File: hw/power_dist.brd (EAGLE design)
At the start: 80 x 50 mm, 82 parts, among them J1 JST-ZH6SMT_VERT, J2 JST-PH4SMT_VERT, J3 JST-PH5VERT, P1 XT30P, P2 XT30P, P3 XT30P, P4 XT30P, P5 XT30P, P6 XT30P, P7 XT90PW-M, Q1 PSMN4R8-100BSEJ, Q2 PSMN4R8-100BSEJ, Q3 PSMN4R8-100BSEJ, Q4 MF-DSC-SOT233-MMBT3904, Q5 MMBT5401 100V, U1 MAX15062AATA+T, U2 STM32G474CEU6, U4 TCAN334G, U5 LT1787HVIMS8PBF, U6 LTC4830

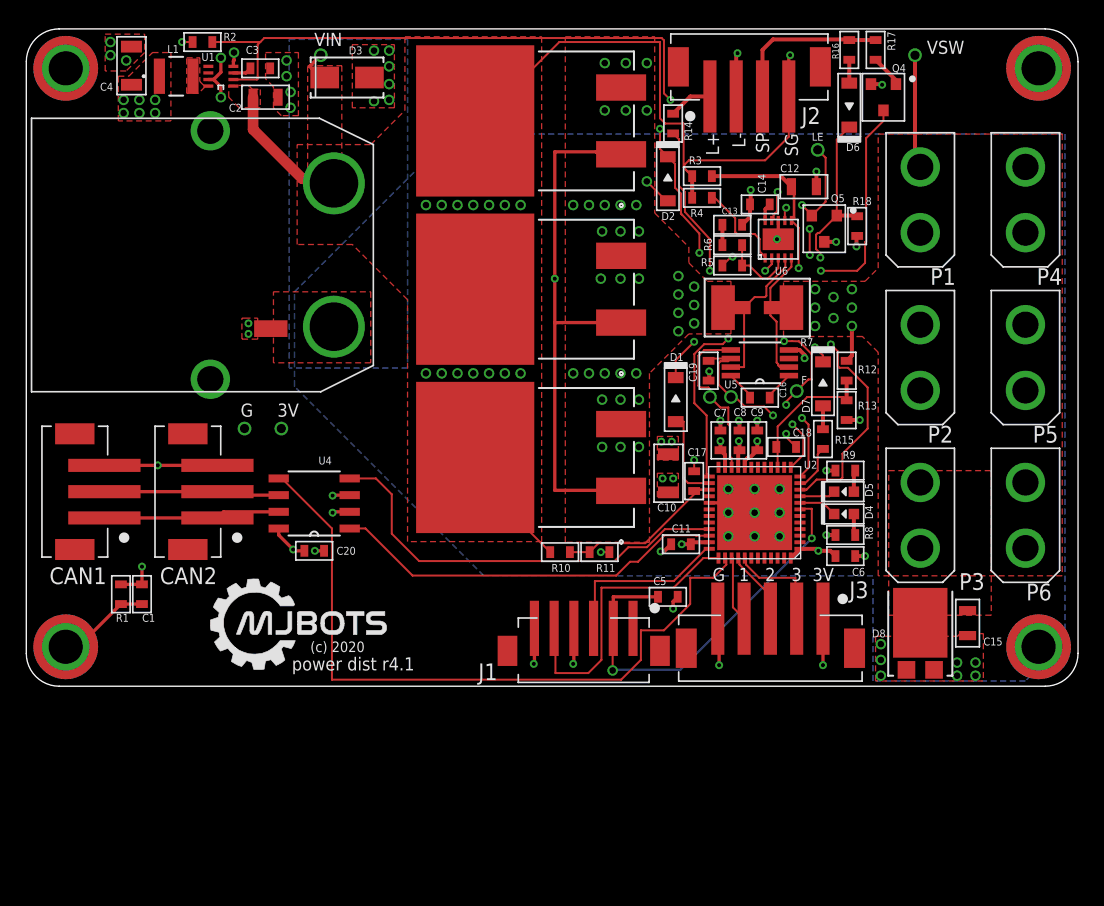
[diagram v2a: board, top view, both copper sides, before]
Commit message: Rough placement of r4.2 with the TPS2490
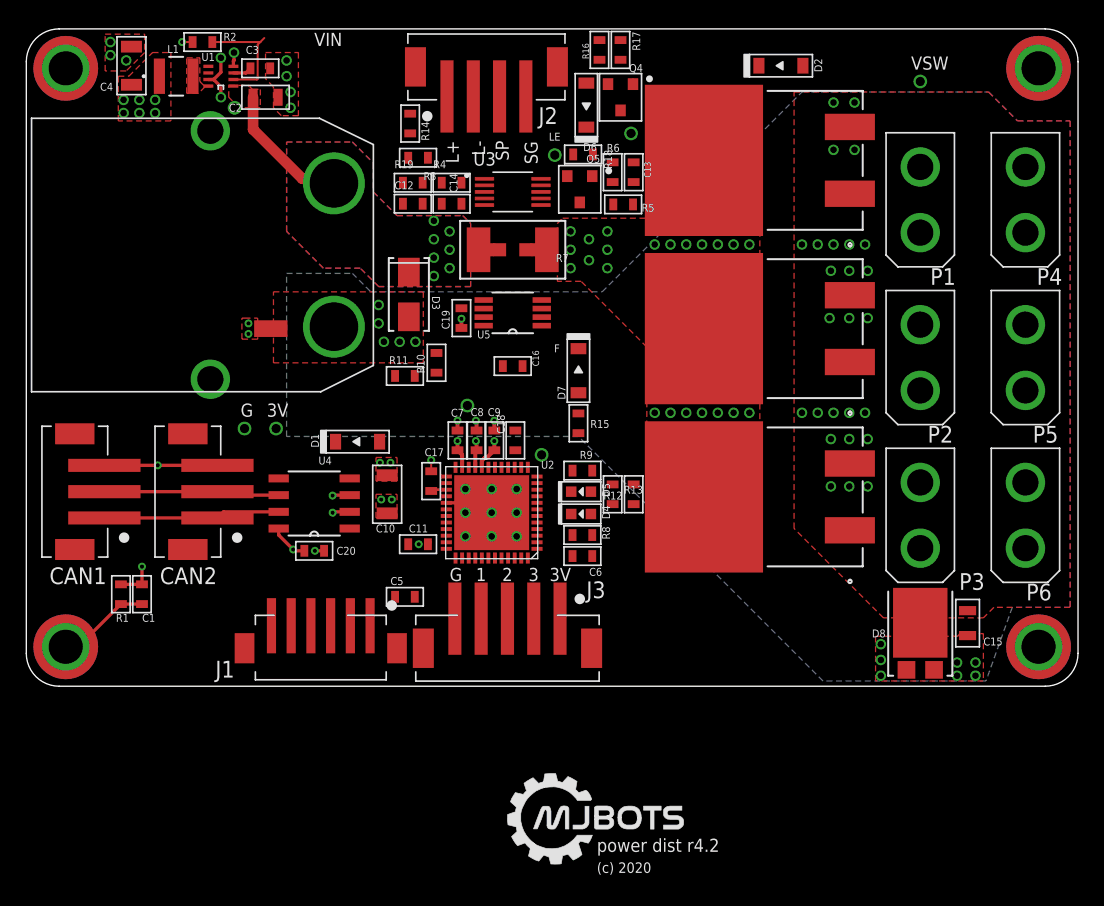
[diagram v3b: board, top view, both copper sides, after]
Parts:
- removed U6: LTC4830, power_dist:DFN10
- added R19: 6.8k 1%, mfpassives:R0603
- added U3: TPS2490DGSR, TPS2490DGSR:SOP50P490X110-10N
- C12: value 1uF 100V -> .1uF 100V; device mfpassives:C0805 -> mfpassives:C0603
- C13: value (none) -> 27nF
- C14: value 0.1uF -> 10nF
- R3: value 10k -> 2M
- R4: value (none) -> 47k 1%
- R5: value (none) -> 10
- R6: value (none) -> 1k
- moved C12 29.8 mm to (29.4, 36.7)
- moved D1 24.4 mm to (25.2, 18.6), turned to 0 degrees
- moved C14 23.5 mm to (32.4, 36.7)
- moved DB_FLT 23.3 mm to (46.0, 42.0)
- moved R3 21.6 mm to (29.8, 40.2), turned to 180 degrees
- moved R18 21.6 mm to (42.4, 40.5), turned to 0 degrees
- moved C10 21.5 mm to (27.4, 14.6)
- moved C18 20.6 mm to (37.2, 18.7), turned to 90 degrees
- moved DB_LEN 20.0 mm to (40.2, 40.4)
- moved J1 20.0 mm to (22.4, 2.60)
- moved R14 20.0 mm to (29.2, 42.8)
- moved C6 20.0 mm to (42.3, 9.90)
- moved C7 20.0 mm to (32.8, 18.7)
- moved C8 20.0 mm to (34.2, 18.7)
- moved C9 20.0 mm to (35.6, 18.7)
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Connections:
- removed net LTC_VCC: C12.P$1, R3.P$2, U6.2, U6.6
- removed net N$10: R4.P$1, U6.1
- removed net N$12: C14.P$1, U6.10
- removed net N$5: R5.P$1, R6.P$2, U6.3
- removed net VIN_POST: D2.ANODE, Q1.3, Q2.3, Q3.3, R7.1
- new net GDRV: R5.P$1, R6.P$2, U3.8
- new net PROG: R19.P$2, R4.P$1, U3.3
- new net TIMER: C14.P$1, U3.4
- new net VREF: R4.P$2, U3.2
- new net VSENSE: Q1.2, Q2.2, Q3.2, R7.2
- net +24V: now also C12.P$1, R3.P$2, R7.1; no longer Q1.2, Q2.2, Q3.2, R3.P$1, R4.P$2
- net FLT: now also U3.6; no longer U6.7
- net GND: now also R19.P$1, U3.5; no longer U6.8, U6.P$1
- net LTC_EN: now also R3.P$1, U3.1; no longer U6.9
- net VSENSE_HIGH: now also U3.10; no longer U6.4
- net VSENSE_LOW: now also U3.9; no longer U6.5
- net VSWITCHED: now also D2.ANODE, Q1.3, Q2.3, Q3.3, U3.7; no longer R7.2
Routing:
- net 3V3_EN: track 71.0 -> 8.83 mm, vias 4 -> 0
- net +24V: track 69.0 -> 10.3 mm, vias 15 -> 7
- net GATE: track 56.3 -> 0.06 mm, vias 2 -> 0
- net CAN_SHDN: track 54.1 -> 0.10 mm
- net SNS_PWR_SW: track 40.3 -> 0.00 mm, vias 2 -> 0
- net CAN_RX: track 32.7 -> 0.00 mm
- net PWR_LED: track 31.5 -> 0.00 mm, vias 2 -> 0
- net NRST: track 31.5 -> 0.23 mm, vias 2 -> 0
- net CAN_TX: track 30.1 -> 0.01 mm
- net FLT: track 26.3 -> 0.00 mm, vias 6 -> 0
- net GND: track 51.3 -> 26.2 mm, vias 48 -> 32
- net N$13: track 22.7 -> 0.00 mm, vias 2 -> 0
- net SWCLK: track 22.7 -> 0.18 mm
- net LTC_VCC: track 16.9 -> 0.00 mm, vias 2 -> 0
- net ISAMP_BIAS: track 16.9 -> 0.25 mm, vias 2 -> 0
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- added copper zone on layer 15, net +24V
- added copper zone on layer 16, net +24V
- added copper zone on layer 1, net VSENSE
- added copper zone on layer 2, net VSENSE
- removed copper zone on layer 1, net VIN_POST
- removed copper zone on layer 2, net VIN_POST
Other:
- board text added: "power dist r4.2"
- board text removed: "power dist r4.1"

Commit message: r4.2 everything rough routed
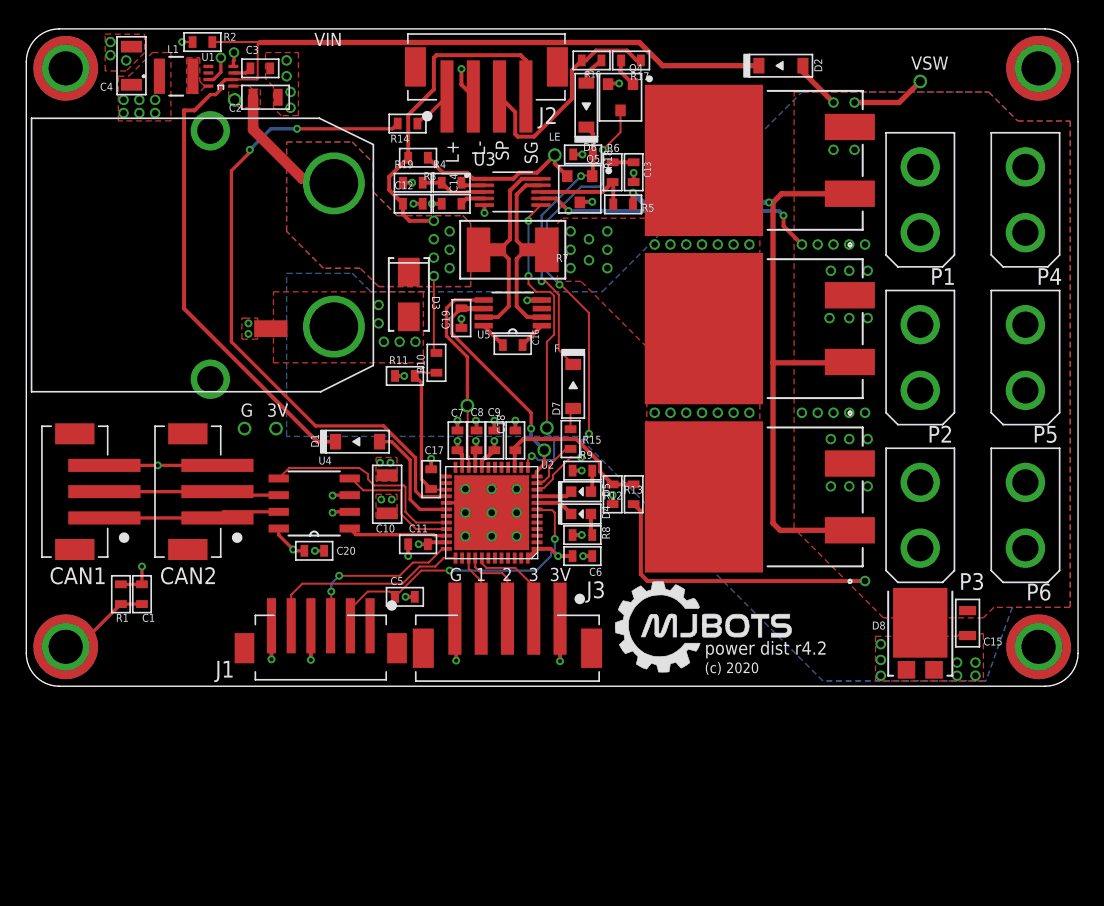
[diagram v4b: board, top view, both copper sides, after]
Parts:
- moved DB_FLT 23.3 mm to (39.6, 19.6)
- moved C16 1.60 mm to (37.0, 25.9)
- moved R15 1.34 mm to (41.4, 18.8)
- moved D7 1.26 mm to (41.6, 22.8)
- moved R17 1.13 mm to (46.0, 47.6), turned to 0 degrees
- moved R16 1.00 mm to (43.0, 47.6), turned to 180 degrees
- moved DB_VIN 0.60 mm to (15.8, 44.6)
- moved DB_IB 0.40 mm to (39.4, 17.9)
- moved R14 0.20 mm to (29.0, 42.8), turned to 180 degrees
- moved C17 0.15 mm to (30.8, 15.8)
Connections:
- net 3V3_OVERRIDE: now also U2.30; no longer U2.26
- net CAN_SHDN: now also U2.32; no longer U2.38
- net PWR_LED: now also U2.28; no longer U2.25
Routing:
- net 3V3_EN: track 8.83 -> 82.8 mm
- net GATE: track 0.06 -> 54.3 mm, vias 0 -> 2
- net VSWITCHED: track 0.00 -> 54.0 mm, vias 26 -> 29
- net PWR_LED: track 0.00 -> 50.0 mm, vias 0 -> 2
- net SNS_PWR_SW: track 0.00 -> 35.7 mm, vias 0 -> 4
- net +24V: track 10.3 -> 42.5 mm
- net FLT: track 0.00 -> 24.5 mm, vias 0 -> 3
- net NRST: track 0.23 -> 23.5 mm, vias 0 -> 2
- net N$13: track 0.00 -> 21.6 mm, vias 0 -> 2
- net GND: track 26.2 -> 44.3 mm, vias 32 -> 49
- net ISAMP_BIAS: track 0.25 -> 18.0 mm, vias 0 -> 1
- net PWR_SW: track 0.07 -> 17.3 mm
- net CAN_SHDN: track 0.10 -> 16.1 mm
- net ISAMP: track 0.00 -> 15.9 mm
- net SWCLK: track 0.18 -> 16.0 mm
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
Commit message: Connect TIMER to an ADC and add a FET temperature sensor
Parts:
- added C21: 0.1uF, mfpassives:C0603
- added U6: STLM20DD9FUDFN-4L_STM-L, power_dist:UDFN-4L_STM-L
- moved DB_FLT 0.40 mm to (39.6, 20.1)
- moved R12 0.15 mm to (46.0, 14.6)
- moved R13 0.05 mm to (44.5, 14.6)
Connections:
- new net FET_TEMP: U2.16, U6.1
- net GND: now also C21.P$2, U6.3
- net TIMER: now also U2.24
- net VCC: now also C21.P$1, U6.4
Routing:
- net FET_TEMP: track 0.00 -> 32.2 mm
- net TIMER: track 1.92 -> 28.2 mm, vias 0 -> 2
- net GND: track 44.3 -> 64.6 mm, vias 49 -> 51
- net VCC: track 23.0 -> 40.7 mm, vias 20 -> 22
- net VSWITCHED: track 54.0 -> 56.2 mm

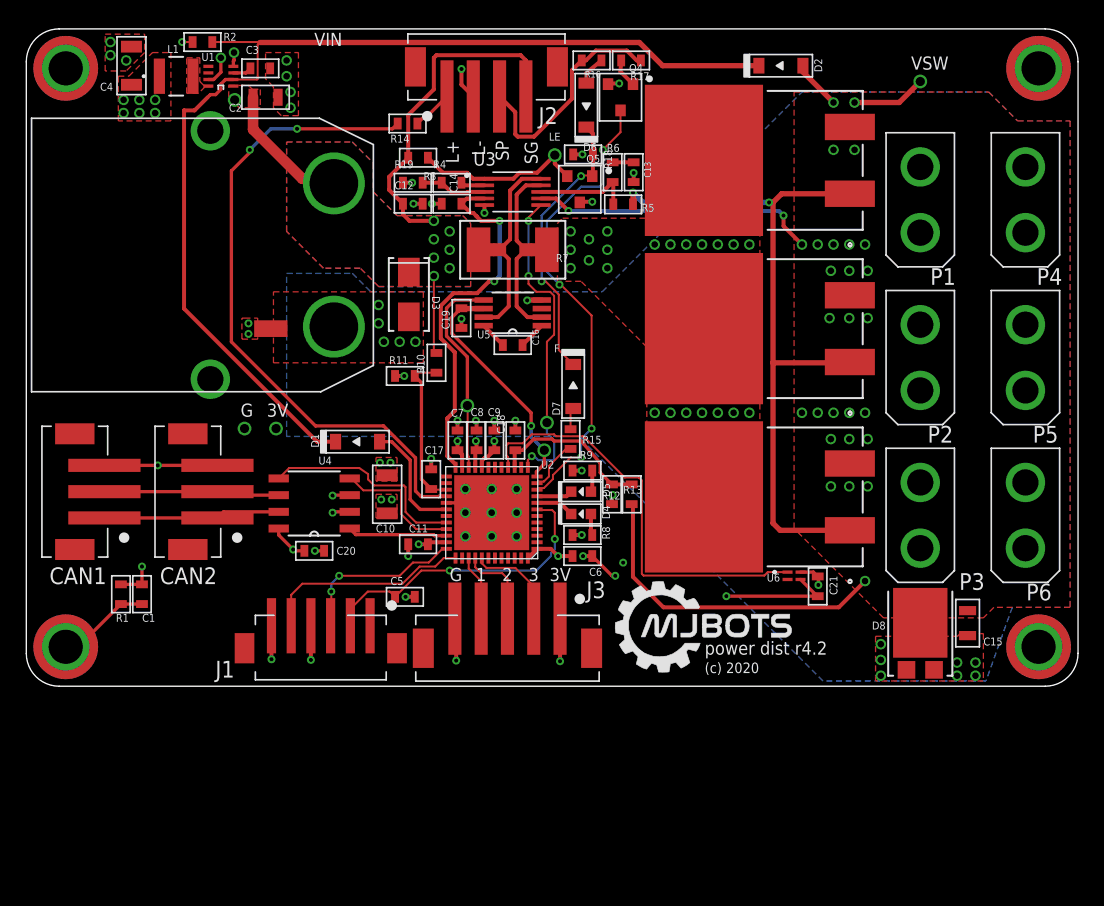
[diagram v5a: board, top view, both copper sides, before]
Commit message: Renumber all resistors and caps
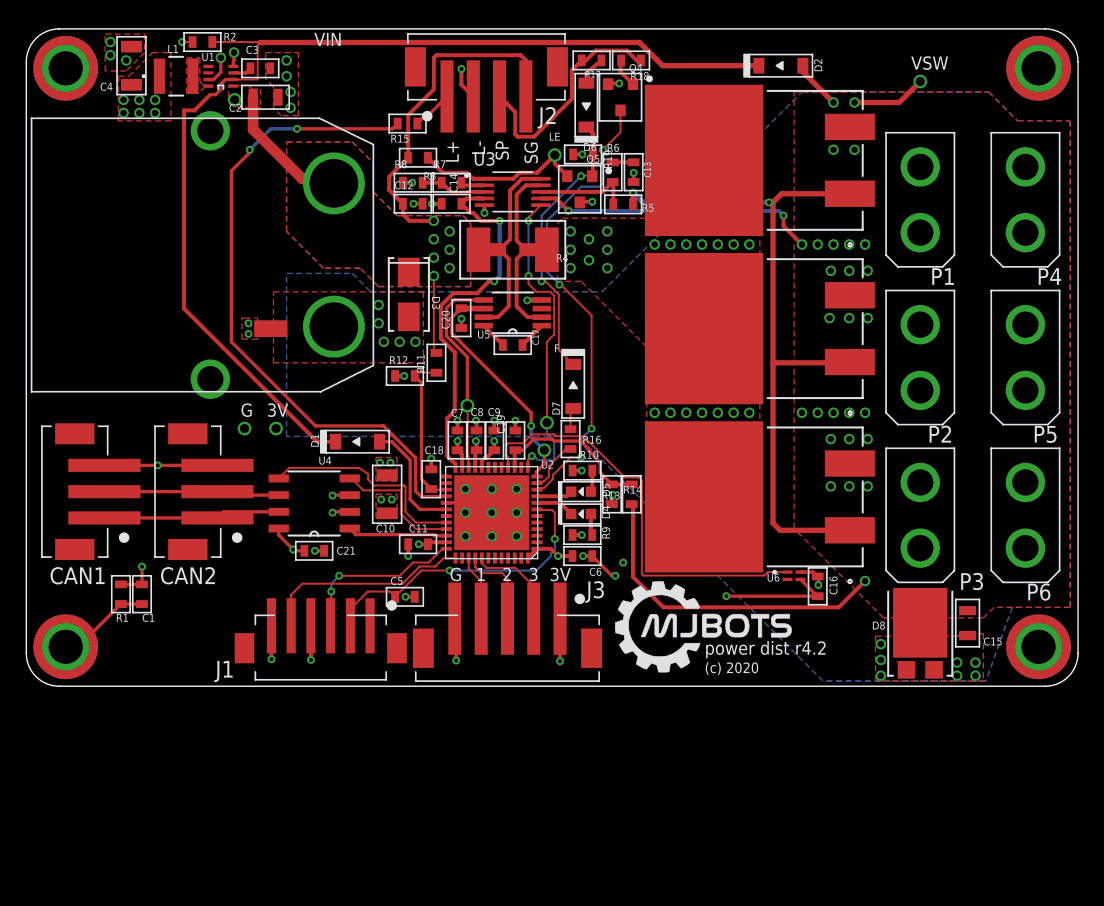
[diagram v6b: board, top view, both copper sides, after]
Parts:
- C16: value DNP -> 0.1uF
- C17: value 0.01uF -> DNP
- C19: value 0.1uF -> 0.01uF
- R10: value 3M 1% -> 220
- R11, R13: value 200k 1% -> 3M 1%
- R12: value 3M 1% -> 200k 1%
- R14: value 220 -> 200k 1%
- R15: value 1k -> 220
- R16: value 500k -> 1k
- R17: value 2M -> 500k
- R18: value 200k -> 2M
- R19: value 6.8k 1% -> 200k
- R4: value 47k 1% -> 0.5mOhm; device mfpassives:R0603 -> power_dist:SHUNT2512
- R7: value 0.5mOhm -> 47k 1%; device power_dist:SHUNT2512 -> mfpassives:R0603
- R8: value 220 -> 6.8k 1%
- moved C21 38.4 mm to (21.9, 10.3), turned to 180 degrees
- moved R14 32.2 mm to (44.5, 14.6), turned to 90 degrees
- moved R8 29.7 mm to (29.4, 38.3), turned to 0 degrees
- moved C16 29.6 mm to (60.2, 7.60), turned to 270 degrees
- moved R16 28.8 mm to (41.4, 18.8), turned to 270 degrees
- moved R15 27.0 mm to (29.0, 42.8), turned to 180 degrees
- moved C20 20.9 mm to (33.1, 28.0), turned to 270 degrees
- moved R12 19.5 mm to (28.8, 23.6), turned to 0 degrees
- moved R10 13.8 mm to (42.3, 16.4), turned to 180 degrees
- moved R19 13.1 mm to (42.4, 40.5)
- moved C17 11.9 mm to (37.0, 25.9), turned to 180 degrees
- moved C19 10.2 mm to (37.2, 18.7), turned to 90 degrees
- moved R18 8.03 mm to (46.0, 47.6)
- moved C18 7.05 mm to (30.8, 15.8)
- moved R4 6.90 mm to (37.0, 33.2)
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- renumbered SH4 to SH1
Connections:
- net +24V: now also R11.P$2, R4.1; no longer R10.P$2, R7.1
- net GND: now also C16.P$2, R12.P$1, R14.P$1, R8.P$1; no longer C17.P$2, R11.P$1, R13.P$1, R18.P$1
- net ISAMP_BIAS: now also C20.P$1; no longer C19.P$1
- net N$11: now also R18.P$1; no longer R17.P$1
- net N$13: now also R19.P$2; no longer R18.P$2
- net N$14: now also R10.P$1; no longer R9.P$1
- net N$17: now also R17.P$1; no longer R16.P$1
- net N$18: now also R16.P$1; no longer R15.P$1
- net N$2: now also R15.P$1; no longer R14.P$1
- net N$6: now also C17.P$1; no longer C16.P$1
- net N$7: now also C17.P$2; no longer C16.P$2
- net N$8: now also R9.P$1; no longer R8.P$1
- net PROG: now also R7.P$1, R8.P$2; no longer R19.P$2, R4.P$1
- net PWR_LED: now also R15.P$2; no longer R14.P$2
- net PWR_OVERRIDE: now also R16.P$2; no longer R15.P$2
- net PWR_SW: now also R18.P$2; no longer R16.P$2
- net VCC: now also C16.P$1, R10.P$2; no longer C20.P$1, R8.P$2
- net VIN_SAMP: now also C18.P$1, R11.P$1, R12.P$2; no longer C17.P$1, R10.P$1, R11.P$2
- net VREF: now also R7.P$2; no longer R4.P$2
- net VSENSE: now also R4.2; no longer R7.2
- net VSENSE_HIGH: now also R4.3; no longer R7.3
- net VSENSE_LOW: now also R4.4; no longer R7.4
- net VSWITCHED: now also R13.P$2; no longer R12.P$2
- net VSWITCHED_SAMP: now also C19.P$1, R13.P$1, R14.P$2; no longer C18.P$1, R12.P$1, R13.P$2

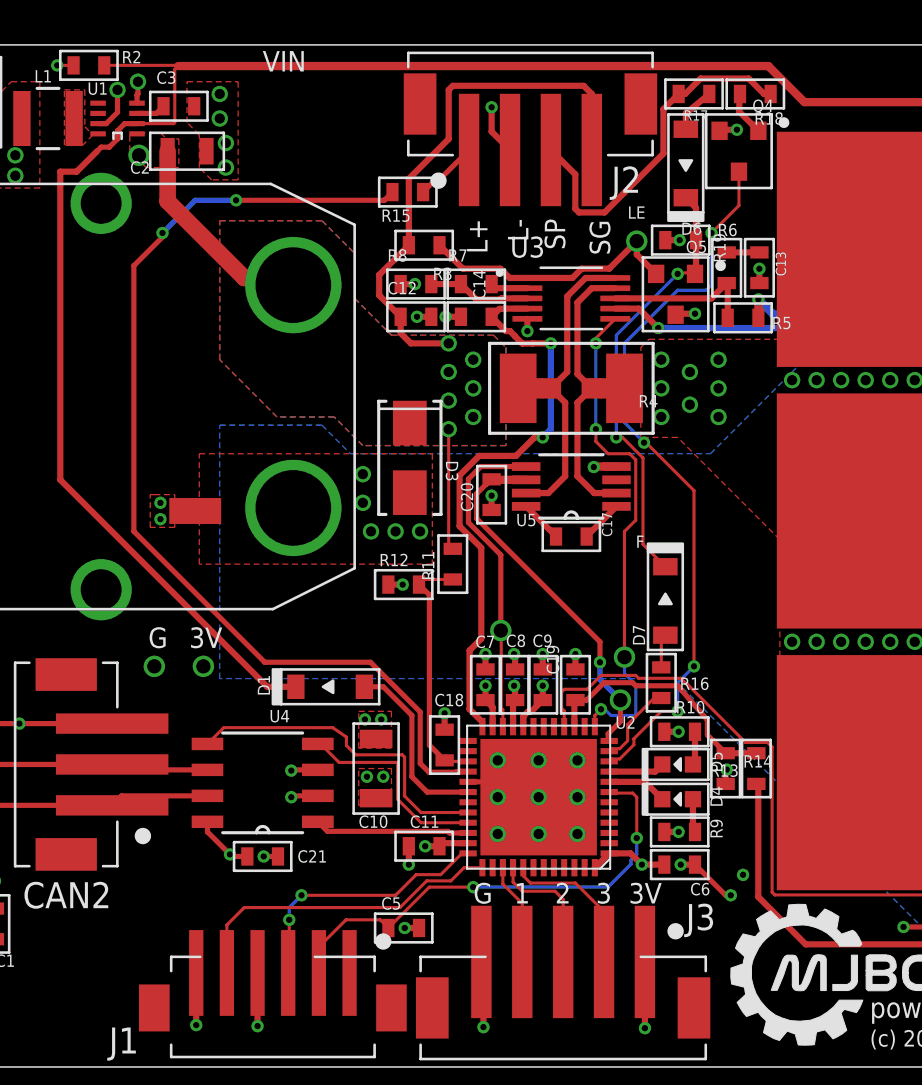
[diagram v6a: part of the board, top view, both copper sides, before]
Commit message: Place all silks and add a few more debug points
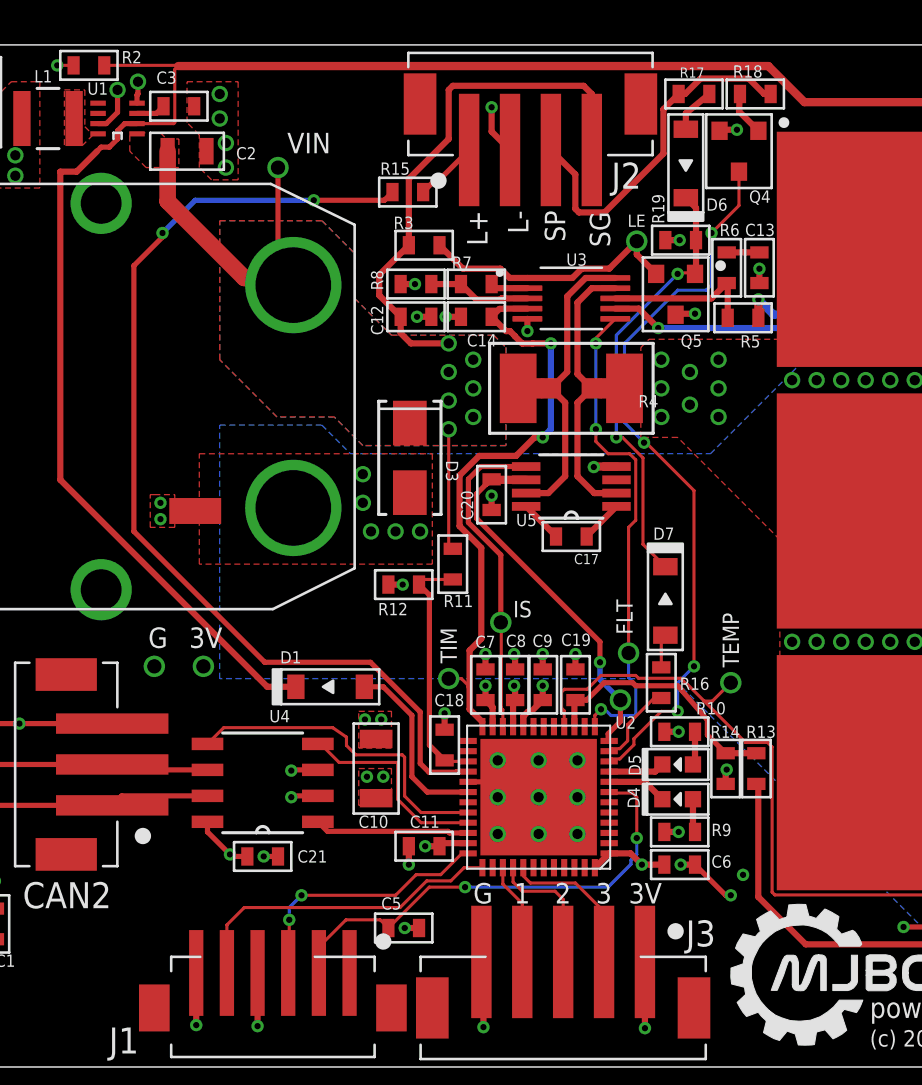
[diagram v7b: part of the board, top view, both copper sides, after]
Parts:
- added DB_TEMP, DB_TIMER: PAD24AWG_PAD, precharge:24AWG_PAD
- moved DB_VIN 6.83 mm to (22.6, 44.0)
- moved DB_IS 0.40 mm to (33.5, 21.8)
- moved DB_FLT 0.28 mm to (39.8, 20.2)
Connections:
- net FET_TEMP: now also DB_TEMP.P$1
- net TIMER: now also DB_TIMER.P$1
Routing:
- net +24V: track 42.5 -> 48.6 mm
- net FET_TEMP: track 32.2 -> 33.9 mm
- net TIMER: track 28.2 -> 29.4 mm
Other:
- board text added: "FLT"
- board text added: "IS"
- board text added: "TEMP"
- board text added: "TIM"
- board text removed: "F"
